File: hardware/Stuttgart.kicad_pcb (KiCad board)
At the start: 2 copper layers, 100 x 50 mm, 66 parts, among them IC1 NCV1117ST33T3G, IC2 UCC12040DVER, IC3 MCP1700T-3302E_TT, IC4 ISO7763DBQR, IC5 ISO7741DBQR, IC6 MCP3202-CI_SN, IC7 MCP251863T-E_9PX, J1 USB_C_Receptacle_USB2.0_16P, J2 FCR7350B, J3 FCR7350G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

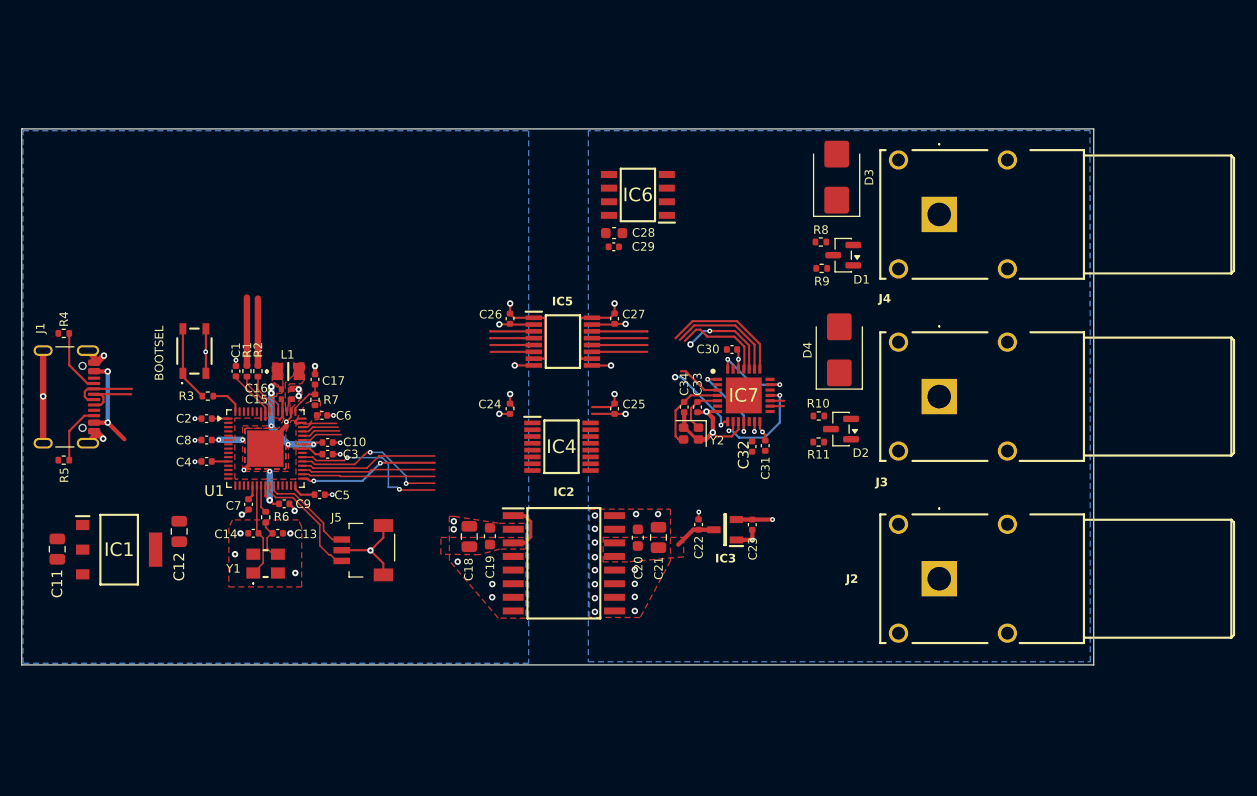
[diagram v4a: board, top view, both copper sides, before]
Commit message: Left hand layout and USB power complete
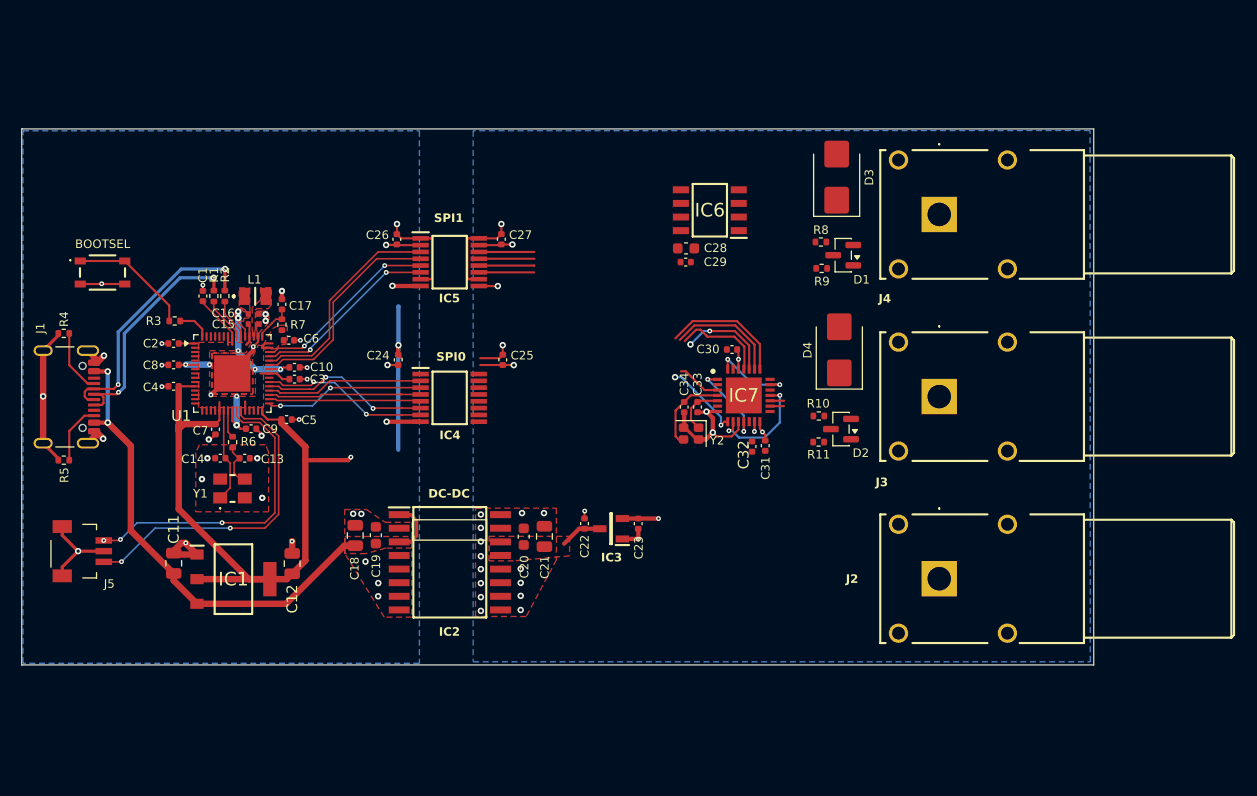
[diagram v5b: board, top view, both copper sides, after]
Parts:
- moved J5 27.1 mm to (108.2, 94.9), turned to -90 degrees
- moved IC5 12.9 mm to (142.9, 67.9)
- moved C26 12.9 mm to (138.0, 65.8)
- moved C27 12.9 mm to (147.7, 65.8)
- moved C24 11.4 mm to (138.1, 77.0)
- moved C25 11.4 mm to (147.9, 77.0)
- moved IC4 11.4 mm to (142.9, 80.6)
- moved S1 11.3 mm to (110.5, 68.9), turned to 0 degrees
- moved IC1 11.0 mm to (122.8, 97.5)
- moved C12 11.0 mm to (128.2, 96.0)
- moved C11 10.9 mm to (117.2, 96.0)
- moved C19 10.6 mm to (136.0, 93.4)
- moved C21 10.6 mm to (151.8, 93.5)
- moved C23 10.6 mm to (160.5, 92.3)
- moved IC3 10.6 mm to (158.0, 92.8)
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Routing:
- net +3V3: track 29.8 -> 100.9 mm, vias 2 -> 3
- net VBUS: track 14.7 -> 49.9 mm
- net /RP2354A/SWD: track 9.09 -> 30.2 mm, vias 0 -> 2
- net /RP2354A/SWCLK: track 11.1 -> 29.0 mm, vias 0 -> 3
- net GND: track 47.1 -> 62.1 mm, vias 32 -> 35
- net SPI1_TX: track 7.78 -> 20.4 mm
- net SPI1_SCK: track 7.90 -> 20.3 mm
- net USB_D-: track 12.2 -> 24.2 mm, vias 0 -> 2
- net SPI1_CS: track 7.39 -> 17.5 mm, vias 0 -> 2
- net USB_D+: track 12.3 -> 22.3 mm, vias 0 -> 2
- net SPI1_RX: track 7.53 -> 17.4 mm, vias 0 -> 2
- net /RP2354A/BOOT_NO: track 7.03 -> 11.8 mm
- net SPI0_CS: track 12.5 -> 14.4 mm
- net SPI0_RX: track 12.4 -> 14.2 mm
- net SPI0_TX: track 13.2 -> 14.9 mm
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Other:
- board text added: "DC-DC"
- board text added: "SPI0"
- board text added: "SPI1"

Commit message: Further CAN controller development
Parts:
- C32: footprint Capacitor_SMD:C_0402_1005Metric -> Capacitor_SMD:C_0603_1608Metric
- moved C30 15.8 mm to (153.6, 78.2)
- moved C32 15.0 mm to (156.3, 87.3), turned to 180 degrees
- moved C31 14.0 mm to (158.5, 87.0)
- moved C34 14.0 mm to (150.9, 83.4)
- moved IC7 14.0 mm to (156.5, 82.3)
- moved C33 14.0 mm to (152.2, 83.4)
- moved Y2 14.0 mm to (151.6, 85.9)
- moved C28 10.9 mm to (154.6, 70.0)
- moved C29 10.9 mm to (154.6, 71.3)
- moved IC6 10.9 mm to (156.8, 66.4)
- moved C23 6.25 mm to (154.6, 90.4), turned to 0 degrees
- moved C22 3.26 mm to (154.5, 95.4), turned to 180 degrees
- moved IC3 2.96 mm to (155.0, 93.0), turned to -90 degrees
- moved C25 1.54 mm to (146.4, 76.8), turned to 90 degrees
- moved C24 1.39 mm to (139.5, 76.8), turned to 90 degrees
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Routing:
- net +3.3VA: track 19.1 -> 59.4 mm, vias 5 -> 6
- net +3V3: track 100.9 -> 114.4 mm, vias 3 -> 4
- net +5V: track 4.73 -> 11.0 mm, vias 1 -> 0
- net SPI0_RX_ISO: track 8.71 -> 14.7 mm
- net SPI0_CS_ISO: track 8.78 -> 14.0 mm
- net CAN_INT1_ISO: track 7.35 -> 12.3 mm
- net CAN_INT_ISO: track 4.14 -> 9.04 mm
- net SPI0_TX_ISO: track 10.6 -> 15.2 mm
- net SPI0_SCK_ISO: track 11.8 -> 15.8 mm
- net GND: track 62.1 -> 60.3 mm
- net GND1: track 24.1 -> 25.0 mm, vias 21 -> 22
- removed copper zone on F.Cu, net +5V

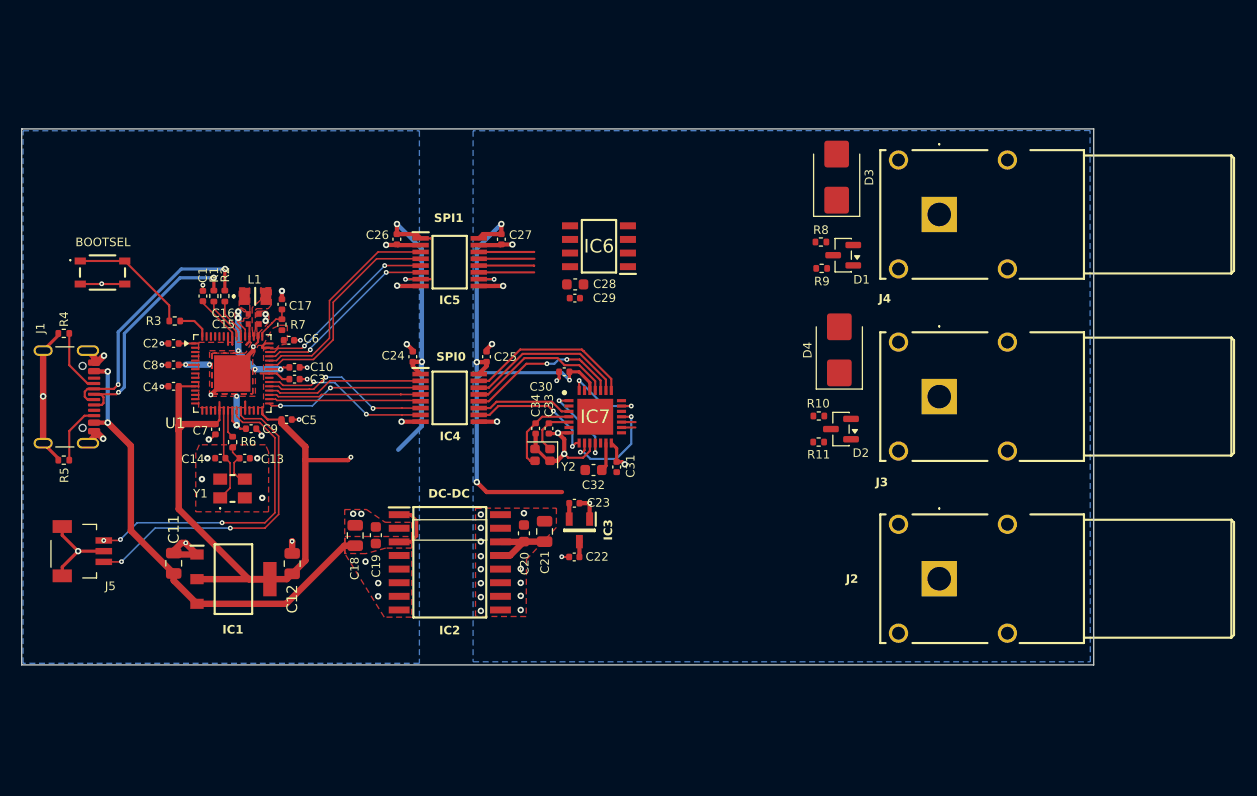
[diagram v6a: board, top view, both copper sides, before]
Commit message: Schematic nearly complete. Board size finalised.
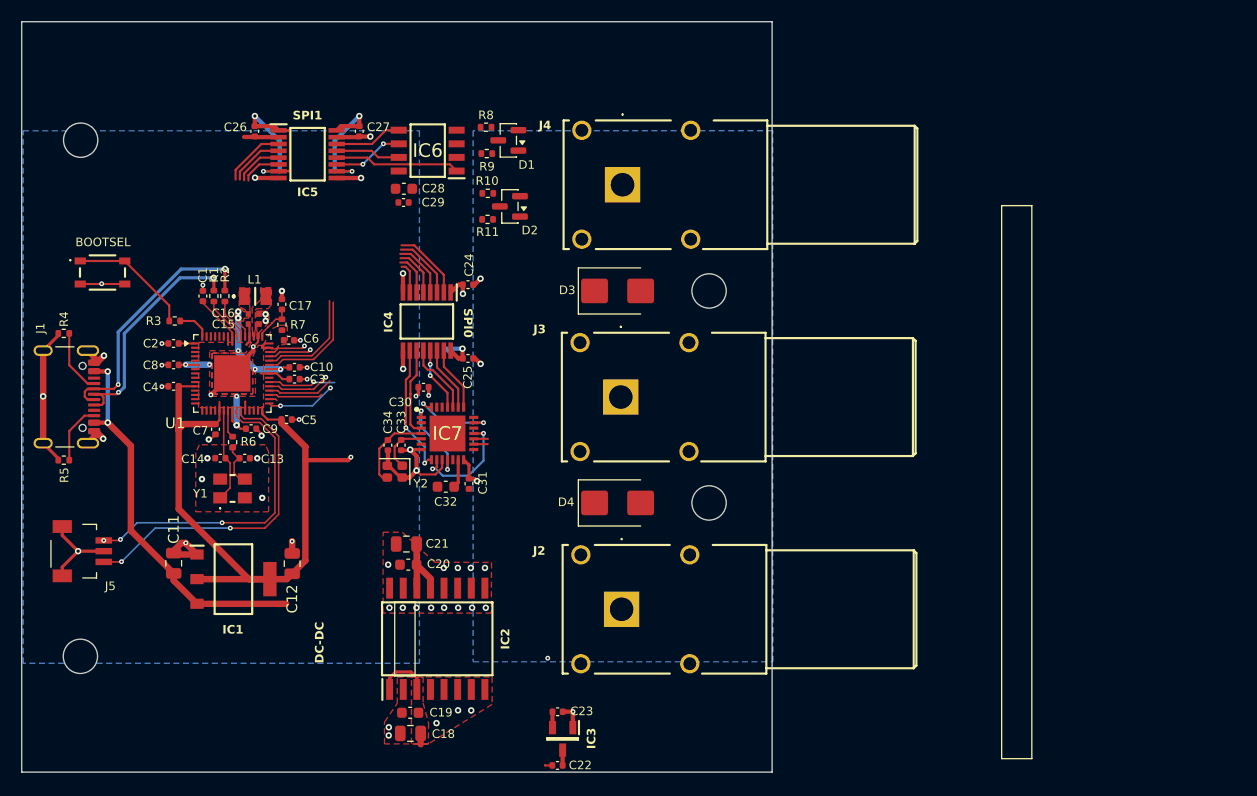
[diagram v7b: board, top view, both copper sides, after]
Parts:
- added H1: MountingHole, MountingHole:MountingHole_3.2mm_M3, F.Cu at (167.1, 90.4)
- added H2: MountingHole, MountingHole:MountingHole_3.2mm_M3, F.Cu at (167.1, 70.6)
- added H3: MountingHole, MountingHole:MountingHole_3.2mm_M3, F.Cu at (108.5, 56.5)
- added H4: MountingHole, MountingHole:MountingHole_3.2mm_M3, F.Cu at (108.5, 104.7)
- moved D2 37.2 mm to (148.5, 62.7)
- moved R10 37.2 mm to (146.5, 61.5)
- moved R11 37.2 mm to (146.5, 63.9)
- moved R9 33.0 mm to (146.4, 57.8)
- moved R8 33.0 mm to (146.3, 55.3)
- moved D1 33.0 mm to (148.4, 56.6)
- moved J2 29.8 mm to (159.0, 100.3)
- moved J3 29.7 mm to (158.9, 80.5)
- moved J4 29.7 mm to (159.1, 60.7)
- moved D4 25.1 mm to (158.6, 90.4), turned to 0 degrees
- moved D3 23.0 mm to (158.6, 70.6), turned to 0 degrees
- moved C23 19.5 mm to (153.0, 109.9)
- moved IC3 19.5 mm to (153.5, 112.4)
- moved C22 19.5 mm to (153.0, 114.9)
- moved C18 19.2 mm to (139.3, 111.9), turned to 180 degrees
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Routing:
- net +3.3VA: track 59.4 -> 22.3 mm, vias 6 -> 5
- net +3V3: track 114.4 -> 97.6 mm
- net SPI0_SCK_ISO: track 15.8 -> 6.04 mm
- net SPI1_RX: track 17.4 -> 7.93 mm, vias 2 -> 1
- net SPI1_CS: track 17.5 -> 7.97 mm, vias 2 -> 1
- net SPI0_TX_ISO: track 15.2 -> 6.10 mm
- net SPI0_RX: track 14.2 -> 5.30 mm
- net SPI0_CS_ISO: track 14.0 -> 5.95 mm, vias 0 -> 2
- net SPI0_RX_ISO: track 14.7 -> 6.68 mm, vias 2 -> 0
- net VBUS: track 49.9 -> 42.2 mm
- net SPI1_CS_ISO: track 5.18 -> 11.7 mm
- net CAN_INT1: track 15.8 -> 9.46 mm, vias 2 -> 1
- net CAN_INT: track 16.0 -> 9.67 mm, vias 2 -> 1
- net SPI1_SCK: track 20.3 -> 15.6 mm
- net SPI1_TX: track 20.4 -> 15.9 mm
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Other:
- board size 100 x 50 mm -> 70 x 70 mm

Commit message: Completed ADC, new components and test points
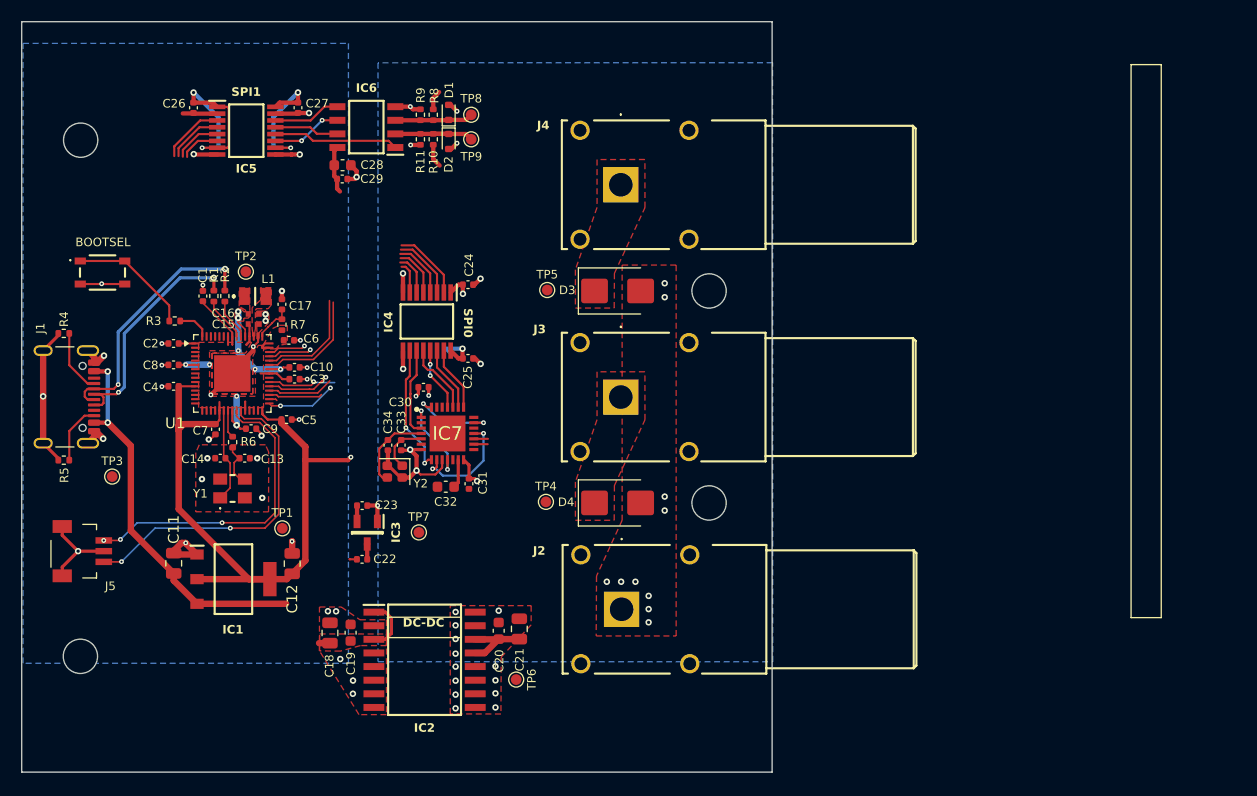
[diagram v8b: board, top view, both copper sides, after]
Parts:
- added TP1: TestPoint, TestPoint:TestPoint_Pad_D1.0mm, F.Cu at (127.3, 92.8)
- added TP2: TestPoint, TestPoint:TestPoint_Pad_D1.0mm, F.Cu at (123.9, 68.8)
- added TP3: TestPoint, TestPoint:TestPoint_Pad_D1.0mm, F.Cu at (111.4, 87.9)
- added TP4: TestPoint, TestPoint:TestPoint_Pad_D1.0mm, F.Cu at (151.9, 90.3)
- added TP5: TestPoint, TestPoint:TestPoint_Pad_D1.0mm, F.Cu at (152.0, 70.5)
- added TP6: TestPoint, TestPoint:TestPoint_Pad_D1.0mm, F.Cu at (149.1, 106.9)
- added TP7: TestPoint, TestPoint:TestPoint_Pad_D1.0mm, F.Cu at (140.1, 93.1)
- added TP8: TestPoint, TestPoint:TestPoint_Pad_D1.0mm, F.Cu at (144.9, 54.2)
- added TP9: TestPoint, TestPoint:TestPoint_Pad_D1.0mm, F.Cu at (144.9, 56.5)
- D1, D2: value BZX84Cxx -> MM5Zxx; footprint Package_TO_SOT_SMD:SOT-23 -> Diode_SMD:D_SOD-523
- moved C23 26.5 mm to (134.8, 90.6)
- moved IC3 26.5 mm to (135.2, 93.2)
- moved C22 26.5 mm to (134.8, 95.7)
- moved C21 13.2 mm to (149.4, 102.1), turned to 90 degrees
- moved C18 12.0 mm to (131.8, 102.5), turned to 90 degrees
- moved C20 10.4 mm to (147.5, 102.3), turned to 90 degrees
- moved R11 9.75 mm to (140.2, 56.5), turned to 90 degrees
- moved C19 9.31 mm to (133.7, 102.5), turned to 90 degrees
- moved D2 8.32 mm to (142.8, 56.7), turned to -90 degrees
- moved R9 7.17 mm to (140.2, 54.2), turned to -90 degrees
- moved R10 7.16 mm to (141.4, 56.5), turned to -90 degrees
- moved D1 6.14 mm to (142.8, 54.0), turned to 90 degrees
- moved C27 6.13 mm to (128.8, 53.5)
- moved C26 6.13 mm to (119.0, 53.5)
- moved C28 6.13 mm to (132.9, 58.9)
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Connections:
- D1 pad 1: GND1 -> /Vehicle Interface/ADC_1
- D1 pad 2: unconnected-(D1-NC-Pad2) -> GND1
- D2 pad 1: GND1 -> /Vehicle Interface/ADC_0
- D2 pad 2: unconnected-(D2-NC-Pad2) -> GND1
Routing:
- net /Vehicle Interface/ADC_0: track 0.00 -> 8.73 mm
- net GND1: track 25.0 -> 32.6 mm, vias 22 -> 36
- net /Vehicle Interface/ADC_1: track 0.00 -> 7.29 mm
- net +3.3VA: track 22.3 -> 26.7 mm
- net /Vehicle Interface/CAN_L: track 1.30 -> 3.49 mm
- net /Vehicle Interface/CAN_H: track 1.32 -> 3.16 mm
- added copper zone on F.Cu, net /Vehicle Interface/CAN_H
- added copper zone on F.Cu, net /Vehicle Interface/CAN_L
